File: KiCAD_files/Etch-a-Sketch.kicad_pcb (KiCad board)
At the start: 2 copper layers, 98 x 85.5 mm, 56 parts, among them J1 Debug Connector, J2 Display / Mounting Socket, J3 Display Mounting Socket, P1 282837-2, SW1 Backlight Select, U1 STM32L433CCTx, U2 W25Q64JV, U3 ICM-42688-P, U6 Adafruit 377 Rotary Encoder, U7 Adafruit 377 Rotary Encoder

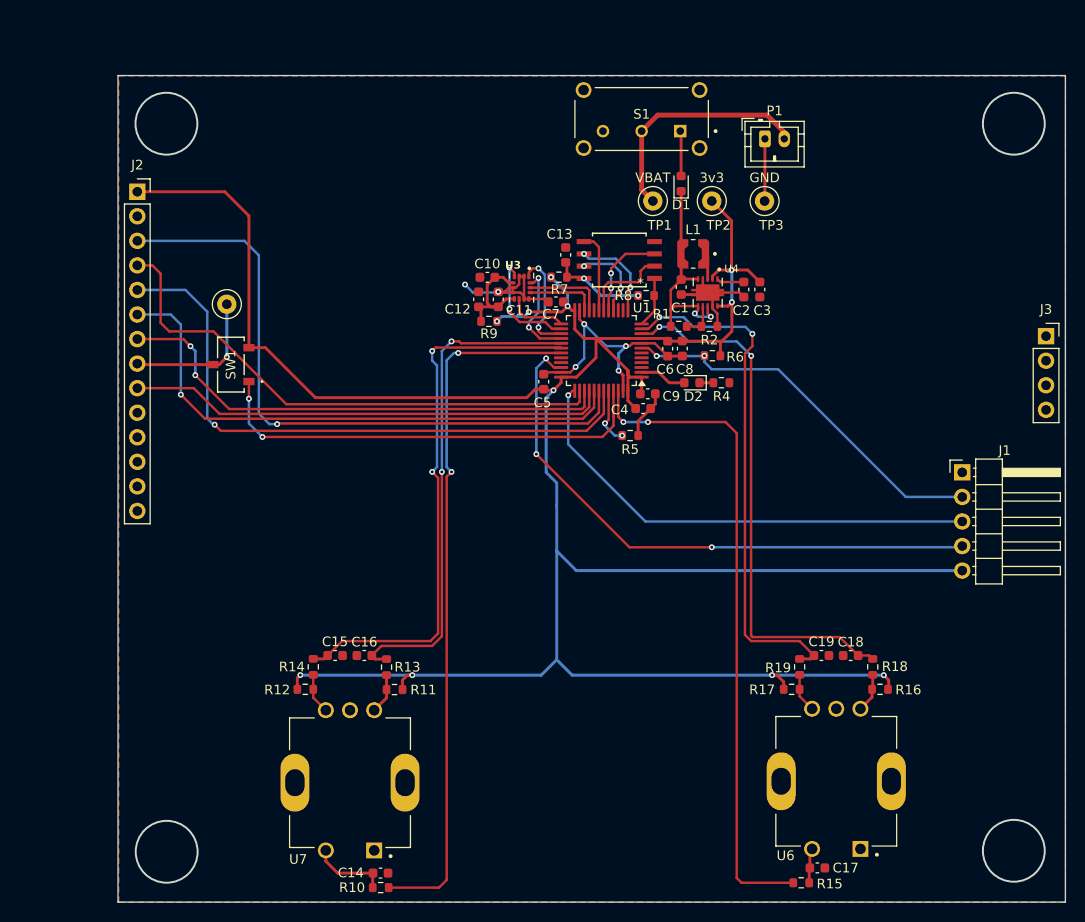
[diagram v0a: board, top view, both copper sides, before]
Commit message: Update Schematic to Rev1
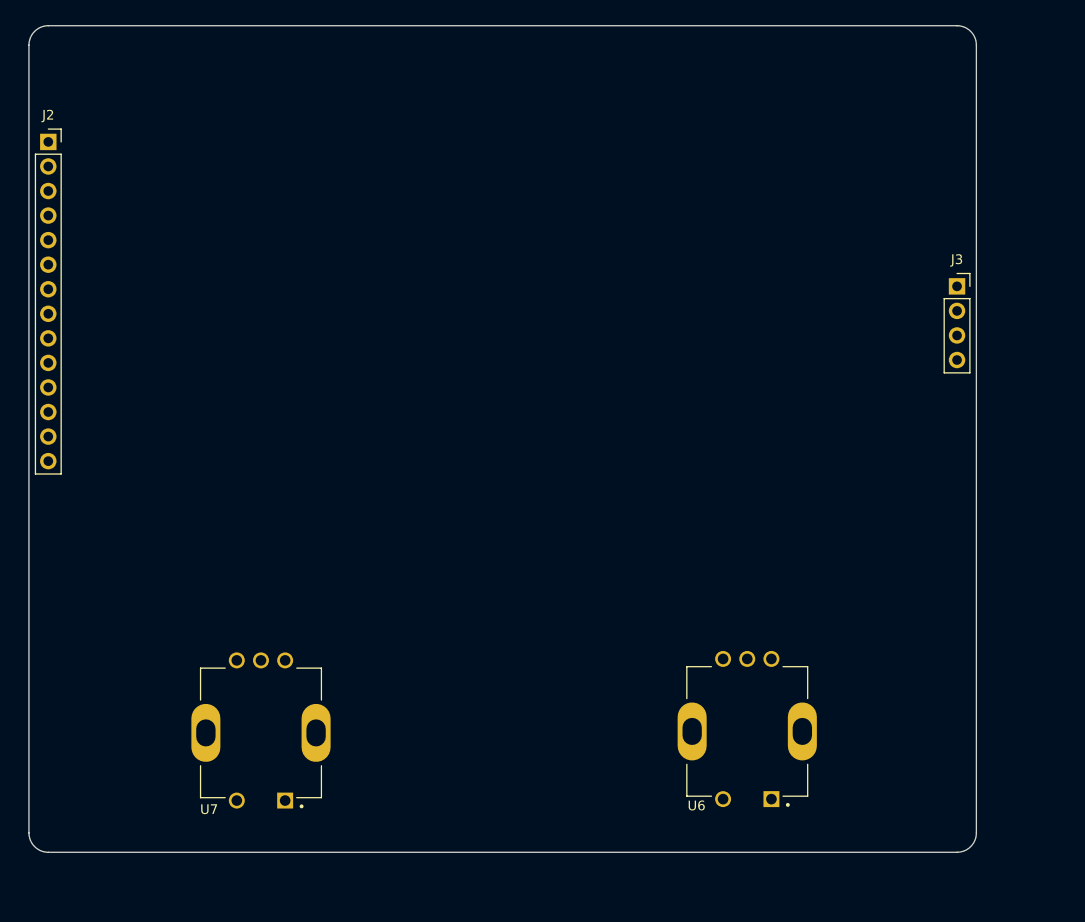
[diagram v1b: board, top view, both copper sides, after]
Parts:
- removed C1, C3: 10uF, Capacitor_SMD:C_0603_1608Metric
- removed C10: 10nF, Capacitor_SMD:C_0603_1608Metric
- removed C11, C13, C2, C4, C5, C6, C7: 0.1uF, Capacitor_SMD:C_0603_1608Metric
- removed C12: 2.2uF, Capacitor_SMD:C_0603_1608Metric
- removed C14, C17: 0.47uF, Capacitor_SMD:C_0603_1608Metric
- removed C15, C16, C18, C19: 0.22uF, Capacitor_SMD:C_0603_1608Metric
- removed C8: 1uF, Capacitor_SMD:C_0603_1608Metric
- removed C9: 4.7uF, Capacitor_SMD:C_0603_1608Metric
- removed D1: D_Schottky, Diode_SMD:D_0603_1608Metric
- removed D2: LED, LED_SMD:LED_0603_1608Metric
- removed J1: Debug Connector, Connector_PinHeader_2.54mm:PinHeader_1x05_P2.54mm_Horizontal
- removed L1: 2.2uH, LPS3015-222MRC:IND_LPS3015-222MRC
- removed P1: 282837-2, Connector_JST:JST_PH_B2B-PH-K_1x02_P2.00mm_Vertical
- removed R1: 2M, Resistor_SMD:R_0603_1608Metric
- removed R10, R11, R12, R13, R14, R15, R16, R17, R18, R19, R8: 10k, Resistor_SMD:R_0603_1608Metric
- removed R2: 250k, Resistor_SMD:R_0603_1608Metric
- removed R4: 220, Resistor_SMD:R_0603_1608Metric
- removed R5, R6: 10K, Resistor_SMD:R_0603_1608Metric
- removed R7, R9: 0, Resistor_SMD:R_0603_1608Metric
- removed S1: EG1224, EG1224:SW_EG1224
- removed SW1: Backlight Select, Switch_footprint:CJS-1200B_NDC
- removed TP1: VBAT, TestPoint:TestPoint_Loop_D1.80mm_Drill1.0mm_Beaded
- removed TP2: 3v3, TestPoint:TestPoint_Loop_D1.80mm_Drill1.0mm_Beaded
- removed TP3: GND, TestPoint:TestPoint_Loop_D1.80mm_Drill1.0mm_Beaded
- removed TP4: LED, TestPoint:TestPoint_Loop_D1.80mm_Drill1.0mm_Beaded
- removed U1: STM32L433CCTx, Package_QFP:LQFP-48_7x7mm_P0.5mm
- removed U2: W25Q64JV, w25_footprints:SOIC-8_5P28X5P28_WIN
- removed U3: ICM-42688-P, ICM_42688_P:PQFN50P300X250X97-14N
- removed U4: ~, TPS61201DRCT:VREG_V62_16624-01YE
- moved J2 10.6 mm to (97.2, 58.9)
- moved J3 10.6 mm to (191.2, 73.8)
- moved U6 10.6 mm to (169.5, 119.9)
- moved U7 10.6 mm to (119.2, 120.0)
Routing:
- net +3V3: track 278.5 -> 0.00 mm, vias 11 -> 0
- net /PB_1: track 72.6 -> 0.00 mm, vias 2 -> 0
- net /SPI3_CS: track 67.9 -> 0.00 mm, vias 1 -> 0
- net /PB_2: track 67.7 -> 0.00 mm, vias 2 -> 0
- net GND: track 67.3 -> 0.00 mm, vias 6 -> 0
- net /DC/RS: track 63.9 -> 0.00 mm, vias 1 -> 0
- net /DEBUG_DIO: track 60.4 -> 0.00 mm, vias 3 -> 0
- net /SPI3_MOCI: track 58.2 -> 0.00 mm, vias 1 -> 0
- net /QEI1_B: track 57.4 -> 0.00 mm, vias 2 -> 0
- net /RESET: track 55.9 -> 0.00 mm
- net /QEI2_A: track 55.4 -> 0.00 mm, vias 2 -> 0
- net /QEI2_B: track 53.8 -> 0.00 mm, vias 2 -> 0
- net /SPI3_SCK: track 52.5 -> 0.00 mm, vias 2 -> 0
- net /QEI1_A: track 52.0 -> 0.00 mm, vias 2 -> 0
- net /DEBUG_CLK: track 50.0 -> 0.00 mm, vias 1 -> 0
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- removed copper zone on F.Cu, net GND
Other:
- outline, holes or cut-outs redrawn
- board text removed: "R10"

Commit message: Initial Rev1 PCB Layout
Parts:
- added C1: 0.1uF, Capacitor_SMD:C_0603_1608Metric, F.Cu at (133.7, 73.2)
- added C10: 0.1uF, Capacitor_SMD:C_0603_1608Metric, F.Cu at (140.1, 69.9)
- added C11: 0.22uF, Capacitor_SMD:C_0603_1608Metric, F.Cu at (114.2, 107.4)
- added C12: 0.22uF, Capacitor_SMD:C_0603_1608Metric, F.Cu at (124.2, 107.4)
- added C13: 0.47uF, Capacitor_SMD:C_0603_1608Metric, F.Cu at (117.1, 129.0)
- added C14: 0.22uF, Capacitor_SMD:C_0603_1608Metric, F.Cu at (174.8, 107.4)
- added C15: 0.22uF, Capacitor_SMD:C_0603_1608Metric, F.Cu at (164.3, 107.4)
- added C16: 0.47uF, Capacitor_SMD:C_0603_1608Metric, F.Cu at (171.0, 129.0)
- added C17: 1uF, Capacitor_SMD:C_0603_1608Metric, F.Cu at (112.3, 51.8)
- added C18: 1uF, Capacitor_SMD:C_0603_1608Metric, F.Cu at (116.8, 51.8)
- added C19: 10uF, Capacitor_SMD:C_0603_1608Metric, F.Cu at (131.1, 52.8)
- added C2: 10uF, Capacitor_SMD:C_0603_1608Metric, F.Cu at (135.3, 73.2)
- added C20: 0.1uF, Capacitor_SMD:C_0603_1608Metric, F.Cu at (151.0, 82.3)
- added C3: 0.1uF, Capacitor_SMD:C_0603_1608Metric, F.Cu at (135.5, 75.7)
- added C4: 0.1uF, Capacitor_SMD:C_0603_1608Metric, F.Cu at (139.1, 83.1)
- added C5: 0.1uF, Capacitor_SMD:C_0603_1608Metric, F.Cu at (149.8, 84.8)
- added C6: 0.1uF, Capacitor_SMD:C_0603_1608Metric, F.Cu at (142.1, 73.4)
- added C7: 10nF, Capacitor_SMD:C_0603_1608Metric, F.Cu at (151.0, 77.8)
- added C8: 1uF, Capacitor_SMD:C_0603_1608Metric, F.Cu at (152.6, 77.8)
- added C9: 4.7uF, Capacitor_SMD:C_0603_1608Metric, F.Cu at (137.6, 83.1)
- added H1: MountingHole, MountingHole:ToolingHole_1.152mm, F.Cu at (97.0, 130.6)
- added H2: MountingHole, MountingHole:ToolingHole_1.152mm, F.Cu at (191.3, 48.8)
- added H3: MountingHole, MountingHole:ToolingHole_1.152mm, F.Cu at (97.0, 48.8)
- added H4: MountingHole, MountingHole:ToolingHole_1.152mm, F.Cu at (191.3, 130.6)
- added J1: Debug Connector, Connector_PinHeader_2.54mm:PinHeader_1x05_P2.54mm_Vertical, F.Cu at (147.3, 94.5)
- added J4: Molex 2171790001, Molex2171790001:2171790001_MOL, F.Cu at (105.7, 50.8)
- added P1: 282837-2, Connector_JST:JST_PH_B2B-PH-K_1x02_P2.00mm_Vertical, F.Cu at (135.4, 53.6)
- added R1: 10K, Resistor_SMD:R_0603_1608Metric, F.Cu at (151.9, 80.0)
- added R10: 10k, Resistor_SMD:R_0603_1608Metric, F.Cu at (172.9, 110.5)
- added R11: 10k, Resistor_SMD:R_0603_1608Metric, F.Cu at (166.1, 109.0)
- added R12: 10k, Resistor_SMD:R_0603_1608Metric, F.Cu at (172.9, 109.0)
- added R13: 10k, Resistor_SMD:R_0603_1608Metric, F.Cu at (167.8, 129.0)
- added R14: 5.1kΩ, Resistor_SMD:R_0603_1608Metric, F.Cu at (108.0, 55.9)
- added R15: 5.1kΩ, Resistor_SMD:R_0603_1608Metric, F.Cu at (103.4, 55.9)
- added R2: 10K, Resistor_SMD:R_0603_1608Metric, F.Cu at (146.9, 86.6)
- added R3: 10k, Resistor_SMD:R_0603_1608Metric, F.Cu at (151.1, 69.7)
- added R4: 10k, Resistor_SMD:R_0603_1608Metric, F.Cu at (115.8, 110.5)
- added R5: 10k, Resistor_SMD:R_0603_1608Metric, F.Cu at (122.5, 110.5)
- added R6: 10k, Resistor_SMD:R_0603_1608Metric, F.Cu at (115.8, 109.0)
- added R7: 10k, Resistor_SMD:R_0603_1608Metric, F.Cu at (122.5, 109.0)
- added R8: 10k, Resistor_SMD:R_0603_1608Metric, F.Cu at (120.2, 129.0)
- added R9: 10k, Resistor_SMD:R_0603_1608Metric, F.Cu at (166.1, 110.5)
- added S1: OS102011MA1QN1, OS102011MA1QN1:OS102011MA1QN1_CNK, F.Cu at (125.5, 49.5)
- added U1: STM32L433CCTx, Package_QFP:LQFP-48_7x7mm_P0.5mm, F.Cu at (145.0, 80.3)
- added U2: W25Q64JV, w25_footprints:SOIC-8_5P28X5P28_WIN, F.Cu at (145.6, 68.7)
- added U3: LIS2DH12TR, LIS2DH12TR:LGA-12_STM, F.Cu at (137.4, 73.7)
- added U4: MCP1700x-300xxTT, Package_TO_SOT_SMD:SOT-23, F.Cu at (114.0, 53.9)
- added VBAT: VBAT, TestPoint:TestPoint_Loop_D1.80mm_Drill1.0mm_Beaded, F.Cu at (137.7, 58.9)
- added VDD: 3v3, TestPoint:TestPoint_Loop_D1.80mm_Drill1.0mm_Beaded, F.Cu at (124.0, 58.9)
- added VSS: GND, TestPoint:TestPoint_Loop_D1.80mm_Drill1.0mm_Beaded, F.Cu at (115.6, 58.9)
- U5: renamed from U7; value Adafruit 377 Rotary Encoder -> PEC11R_4215F_S0024
- U6: value Adafruit 377 Rotary Encoder -> PEC11R_4215F_S0024
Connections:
- J2 pad 8: /LED -> /LED_PWM
- U5 pad S1: (no net) -> GND
- U5 pad S2: (no net) -> GND
- U6 pad S1: (no net) -> GND
- U6 pad S2: (no net) -> GND
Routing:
- net +3V3: track 0.00 -> 232.7 mm, vias 0 -> 8
- net GND: track 0.00 -> 126.7 mm, vias 0 -> 13
- net /SPI3_CS: track 0.00 -> 70.4 mm, vias 0 -> 2
- net /DC/RS: track 0.00 -> 66.8 mm, vias 0 -> 2
- net /LED_PWM: track 0.00 -> 63.1 mm, vias 0 -> 2
- net /SPI3_MOCI: track 0.00 -> 62.9 mm, vias 0 -> 4
- net /RESET: track 0.00 -> 62.0 mm, vias 0 -> 4
- net /PB_1: track 0.00 -> 60.8 mm, vias 0 -> 2
- net /PB_2: track 0.00 -> 57.7 mm
- net /SPI3_SCK: track 0.00 -> 57.0 mm, vias 0 -> 4
- net /SPI3_MICO: track 0.00 -> 54.1 mm, vias 0 -> 4
- net /QEI2_A: track 0.00 -> 47.4 mm, vias 0 -> 2
- net /QEI1_B: track 0.00 -> 45.7 mm, vias 0 -> 2
- net /QEI2_B: track 0.00 -> 40.0 mm, vias 0 -> 2
- net /QEI1_A: track 0.00 -> 38.9 mm, vias 0 -> 2
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- added copper zone on B.Cu, net GND

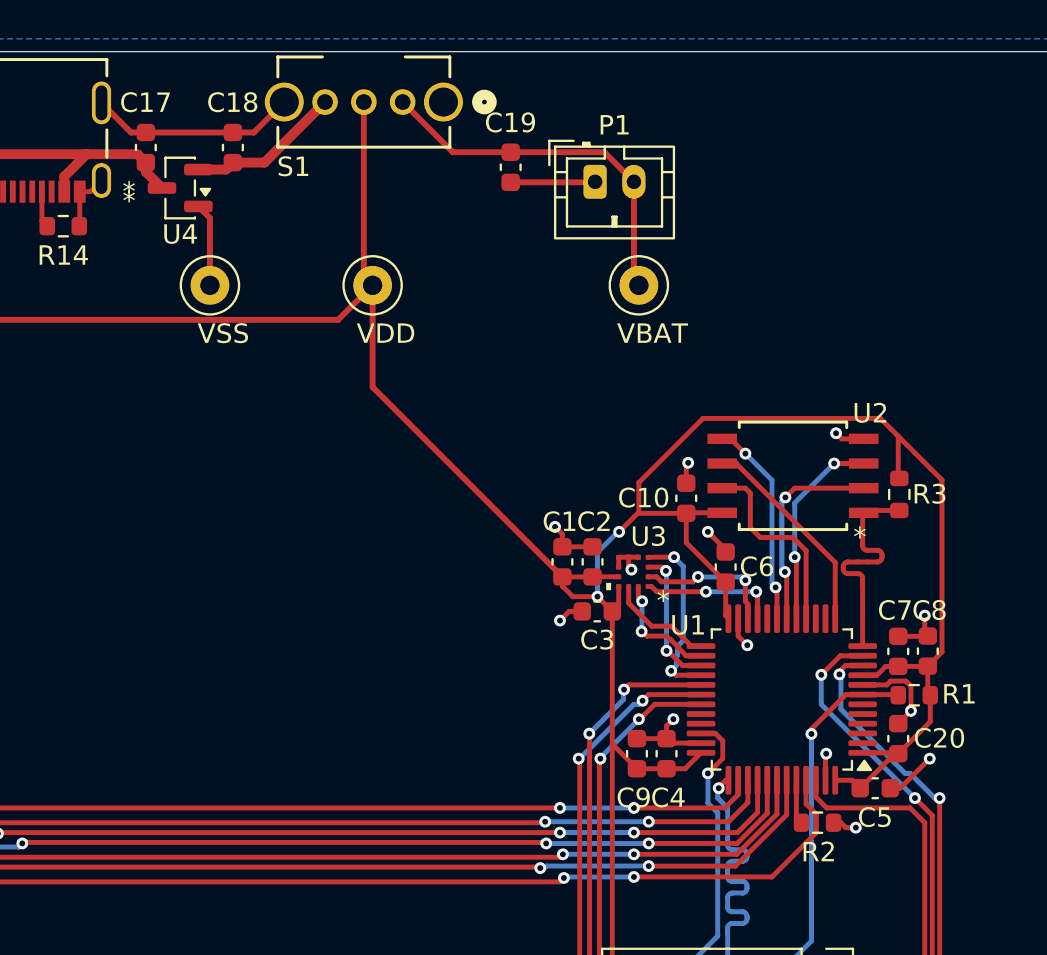
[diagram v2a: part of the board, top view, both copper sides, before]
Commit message: Change Accelerometer IC
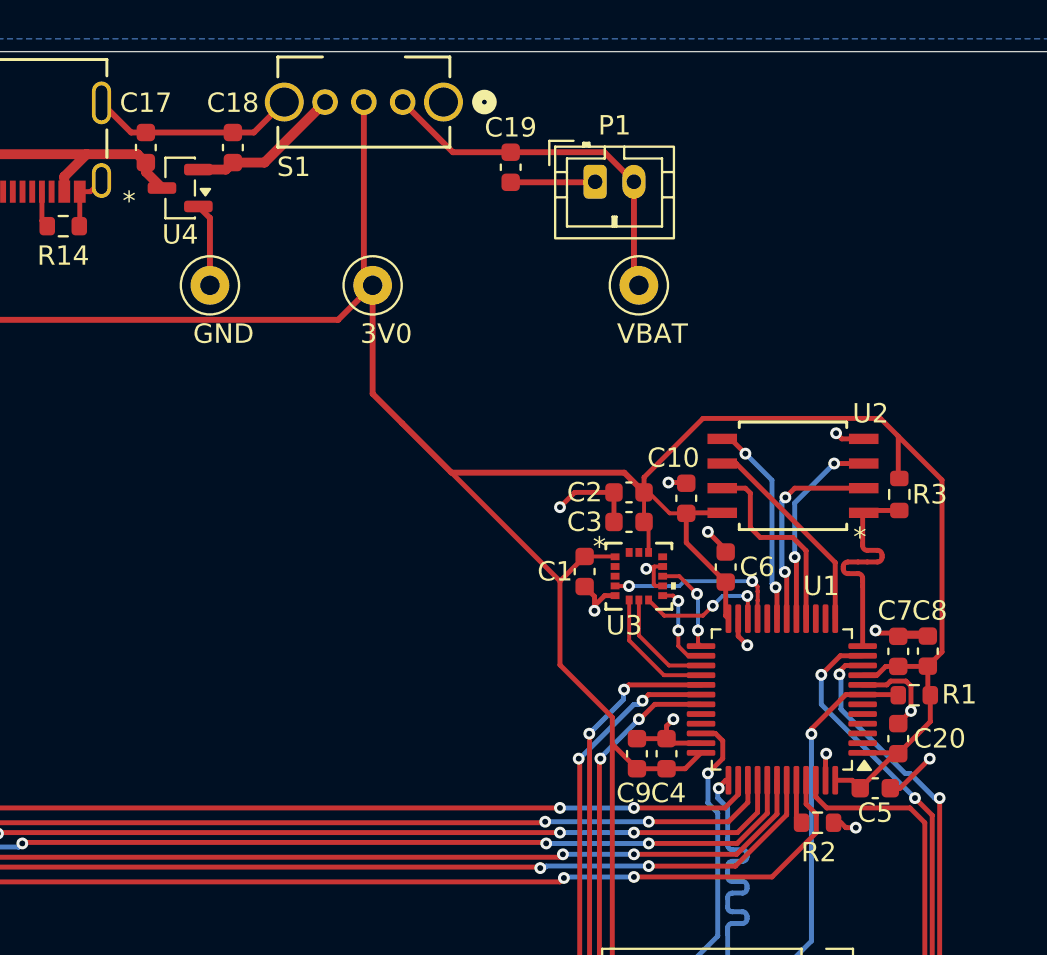
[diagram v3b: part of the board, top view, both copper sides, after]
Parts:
- C2: value 10uF -> 0.1uF
- C3: value 0.1uF -> 10uF
- U3: value LIS2DH12TR -> LIS3DHTR; footprint LIS2DH12TR:LGA-12_STM -> LIS3DHTR:LGA-16_3x3x1mm_STM
- moved C3 4.89 mm to (137.2, 71.1)
- moved C2 4.04 mm to (137.2, 69.6), turned to 180 degrees
- moved C1 1.25 mm to (134.9, 73.7), turned to -90 degrees
- moved U3 0.35 mm to (137.7, 73.9), turned to 0 degrees
- renumbered VDD to 3V0, VSS to GND
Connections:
- U1 pad 25: /ACC_INT2 -> /ACC_INT1
- U1 pad 26: /ACC_INT1 -> /ACC_INT2
- U3 pad 1: /SPI2_SCK -> +3V3
- U3 pad 10: +3V3 -> GND
- U3 pad 11: /ACC_INT2 -> /ACC_INT1
- U3 pad 12: /ACC_INT1 -> GND
- U3 pad 2: /SPI2_CS -> unconnected-(U3-NC-Pad2)
- U3 pad 3: /SPI2_MICO -> unconnected-(U3-NC-Pad3)
- U3 pad 4: /SPI2_MOCI -> /SPI2_SCK
- U3 pad 6: GND -> /SPI2_MOCI
- U3 pad 7: GND -> /SPI2_MICO
- U3 pad 8: GND -> /SPI2_CS
- U3 pad 9: +3V3 -> /ACC_INT2
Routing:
- net +3V3: track 232.7 -> 241.9 mm, vias 8 -> 6
- net GND: track 126.7 -> 131.8 mm
- net /SPI2_MOCI: track 9.27 -> 6.53 mm, vias 2 -> 0
- net /SPI2_SCK: track 7.09 -> 9.23 mm
- net /SPI2_MICO: track 7.21 -> 5.67 mm, vias 2 -> 0
- net /ACC_INT1: track 6.01 -> 4.92 mm
- net /ACC_INT2: track 5.49 -> 4.63 mm, vias 0 -> 2
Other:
- board text added: "*"
